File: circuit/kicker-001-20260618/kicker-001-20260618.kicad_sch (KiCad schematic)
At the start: 64 parts, among them J1 Solenoid_{Stroke}, J2 Solenoid_{Chip}, J3 Drribler_{Front}, J4 Conn_Relay, J6 Voltmeter, Q1 BSS138, Q2 TJ15S06M3L, Q3 Q_Photo_CE, Q4 MTB010N06RJ3, Q5 MTB010N06RJ3, U1 NOT, U10 TLP2361, U11 AND, U12 AND, U2 TLP2361, U3 XL6009E1, U4 NOT, U5 NOT, U6 DRV8874, U7 NOT, U8 NOT, U9 TLP2361

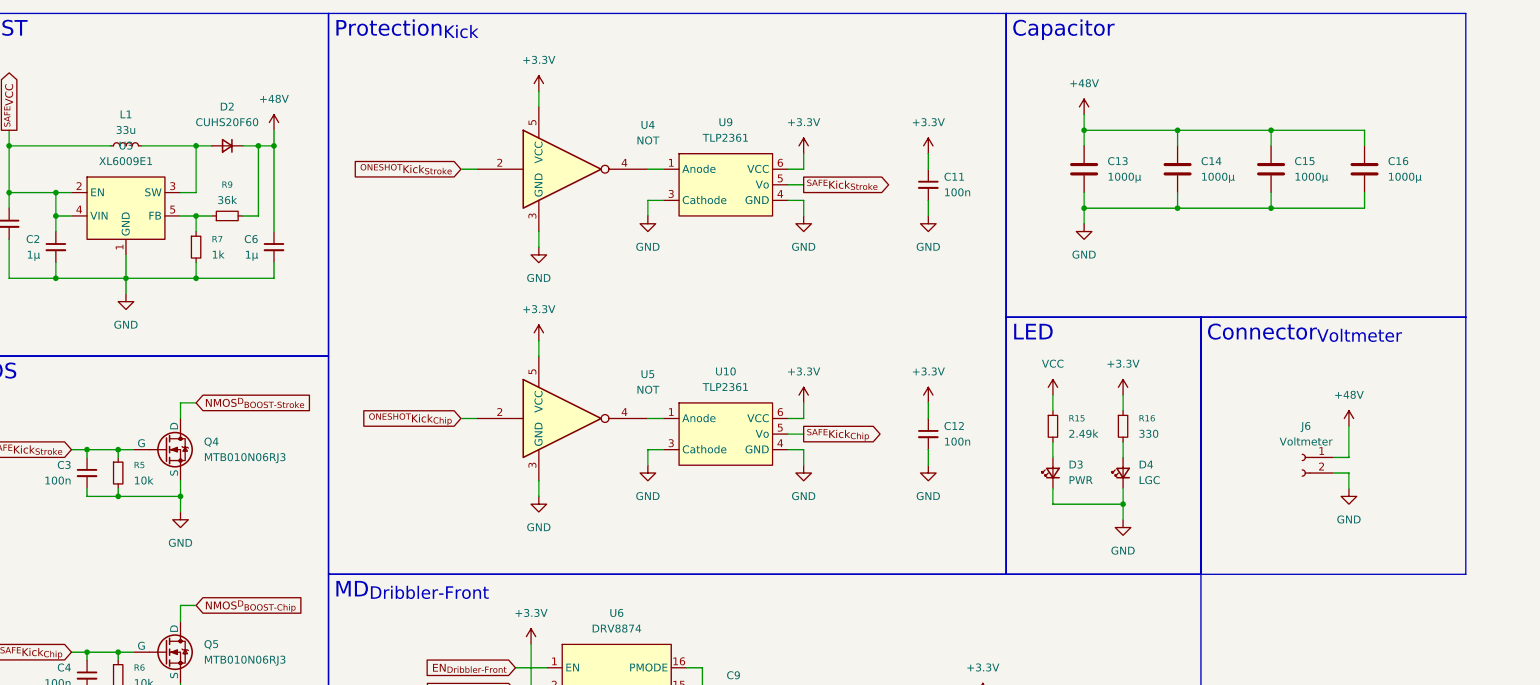
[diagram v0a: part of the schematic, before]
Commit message: Update キッカー基板のボード図完成させた、DRは一日おいてから
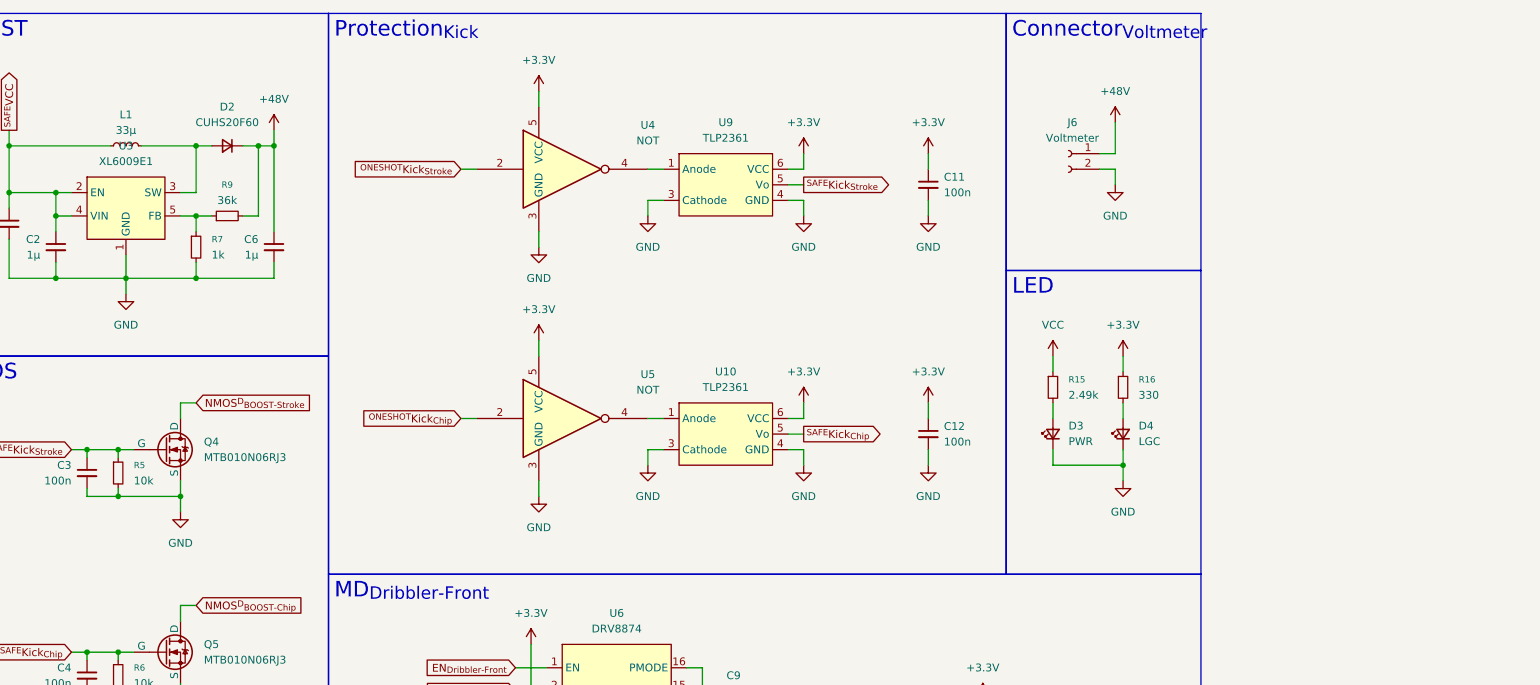
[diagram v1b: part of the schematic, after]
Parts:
- removed C13, C14, C15, C16: 1000μ, Capacitor_THT:C_Radial_D12.5mm_H25.0mm_P5.00mm, symbol Device:C
- C1, C10, C11, C12, C2, C3, C4, C5, C6, C7, C8, C9: footprint Capacitor_SMD:C_0603_1608Metric -> Capacitor_SMD:C_0805_2012Metric
- L1: value 33u -> 33μ
- R1, R10, R11, R12, R13, R14, R15, R16, R17, R2, R3, R4, R5, R6, R7, R8, R9: footprint Resistor_SMD:R_0603_1608Metric -> Resistor_SMD:R_0805_2012Metric
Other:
- moved on the sheet: D3, D4, J6, R15, R16

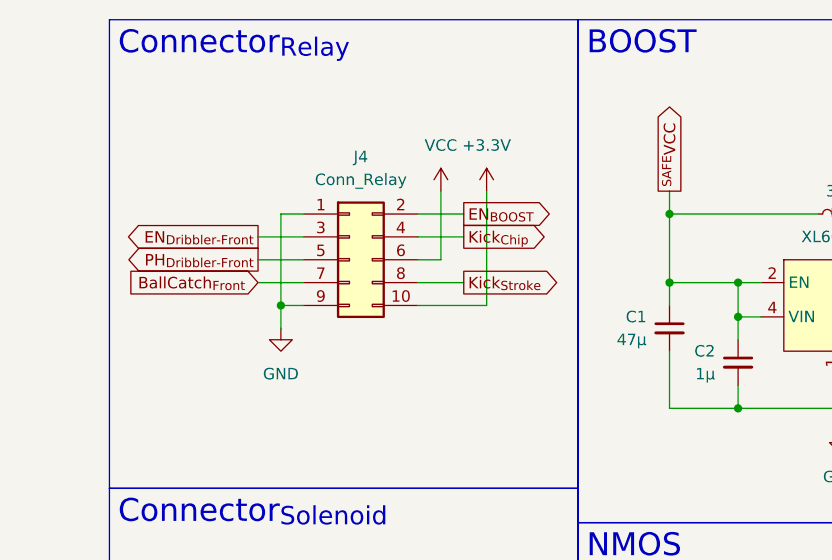
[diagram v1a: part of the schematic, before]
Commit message: Update キッカー基板のピンソケット→ピンヘッダ変更
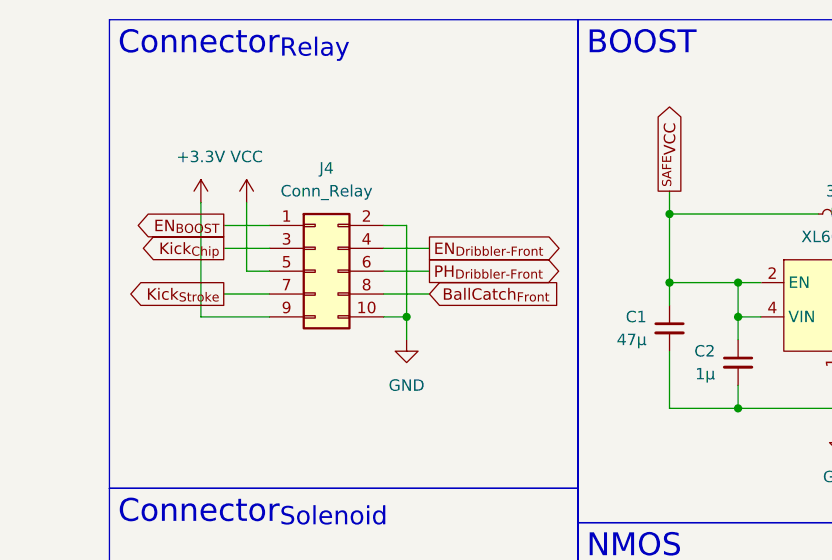
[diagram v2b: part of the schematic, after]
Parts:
- J4: footprint Connector_PinSocket_2.54mm:PinSocket_2x05_P2.54mm_Vertical -> Connector_PinHeader_2.54mm:PinHeader_2x05_P2.54mm_Vertical
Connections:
- net +3.3V: now also J4.9 (Pin_9); no longer J4.10 (Pin_10)
- net BallCatch_{Front}: now also J4.8 (Pin_8); no longer J4.7 (Pin_7)
- net EN_{BOOST}: now also J4.1 (Pin_1); no longer J4.2 (Pin_2)
- net EN_{Dribbler-Front}: now also J4.4 (Pin_4); no longer J4.3 (Pin_3)
- net GND: now also J4.10 (Pin_10), J4.2 (Pin_2); no longer J4.1 (Pin_1), J4.9 (Pin_9)
- net Kick_{Chip}: now also J4.3 (Pin_3); no longer J4.4 (Pin_4)
- net Kick_{Stroke}: now also J4.7 (Pin_7); no longer J4.8 (Pin_8)
- net PH_{Dribbler-Front}: now also J4.6 (Pin_6); no longer J4.5 (Pin_5)
- net VCC: now also J4.5 (Pin_5); no longer J4.6 (Pin_6)
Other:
- moved on the sheet: J4
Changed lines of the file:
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@@
 	)
 	(junction
-		(at 31.75 44.45)
+		(at 45.72 45.72)
 		(diameter 0)
 		(color 0 0 0 0)
@@
 	(wire
 		(pts
-			(xy 46.99 34.29) (xy 52.07 34.29)
+			(xy 30.48 35.56) (xy 25.4 35.56)
 		)
 		(stroke
@@
 	(wire
 		(pts
-			(xy 46.99 44.45) (xy 54.61 44.45)
+			(xy 30.48 45.72) (xy 22.86 45.72)
 		)
 		(stroke
@@
 	(wire
 		(pts
-			(xy 49.53 31.75) (xy 49.53 39.37)
+			(xy 27.94 33.02) (xy 27.94 40.64)
 		)
 		(stroke
@@
 	(wire
 		(pts
-			(xy 29.21 39.37) (xy 34.29 39.37)
+			(xy 48.26 40.64) (xy 43.18 40.64)
 		)
 		(stroke
@@
 	(wire
 		(pts
-			(xy 49.53 39.37) (xy 46.99 39.37)
+			(xy 27.94 40.64) (xy 30.48 40.64)
 		)
 		(stroke
@@
 	(wire
 		(pts
-			(xy 31.75 34.29) (xy 31.75 44.45)
+			(xy 45.72 35.56) (xy 45.72 45.72)
 		)
 		(stroke
@@
 	(wire
 		(pts
-			(xy 52.07 36.83) (xy 46.99 36.83)
+			(xy 25.4 38.1) (xy 30.48 38.1)
 		)
 		(stroke
@@
 	(wire
 		(pts
-			(xy 31.75 44.45) (xy 31.75 46.99)
+			(xy 45.72 45.72) (xy 45.72 48.26)
 		)
 		(stroke
@@
 	(wire
 		(pts
-			(xy 29.21 36.83) (xy 34.29 36.83)
+			(xy 48.26 38.1) (xy 43.18 38.1)
 		)
 		(stroke
@@
 	(wire
 		(pts
-			(xy 34.29 34.29) (xy 31.75 34.29)
+			(xy 43.18 35.56) (xy 45.72 35.56)
 		)
 		(stroke
@@
 	(wire
 		(pts
-			(xy 54.61 31.75) (xy 54.61 44.45)
+			(xy 22.86 33.02) (xy 22.86 45.72)
 		)
 		(stroke
@@
 	(wire
 		(pts
-			(xy 31.75 44.45) (xy 34.29 44.45)
+			(xy 45.72 45.72) (xy 43.18 45.72)
 		)
 		(stroke
@@
 	(wire
 		(pts
-			(xy 52.07 41.91) (xy 46.99 41.91)
+			(xy 25.4 43.18) (xy 30.48 43.18)
 		)
 		(stroke
@@
 	(wire
 		(pts
-			(xy 29.21 41.91) (xy 34.29 41.91)
+			(xy 48.26 43.18) (xy 43.18 43.18)
 		)
 		(stroke
@@
 	(global_label "PH_{Dribbler-Front}"
 		(shape output)
-		(at 29.21 39.37 180)
+		(at 48.26 40.64 0)
 		(fields_autoplaced yes)
 		(effects
@@
 				(size 1.27 1.27)
 			)
-			(justify right)
+			(justify left)
 		)
 		(property "Intersheetrefs" "${INTERSHEET_REFS}"
-			(at 15.1056 39.37 0)
+			(at 62.3644 40.64 0)
 			(hide yes)
 			(show_name no)
@@
 					(size 1.27 1.27)
 				)
-				(justify right)
+				(justify left)
 			)
 		)
@@
 	(global_label "EN_{BOOST}"
 		(shape output)
-		(at 52.07 34.29 0)
+		(at 25.4 35.56 180)
 		(fields_autoplaced yes)
 		(effects
@@
 				(size 1.27 1.27)
 			)
-			(justify left)
+			(justify right)
 		)
 		(property "Intersheetrefs" "${INTERSHEET_REFS}"
-			(at 62.0167 34.29 0)
+			(at 15.4533 35.56 0)
 			(hide yes)
 			(show_name no)
@@
 					(size 1.27 1.27)
 				)
-				(justify left)
+				(justify right)
 			)
 		)
@@
 	(global_label "EN_{Dribbler-Front}"
 		(shape output)
-		(at 29.21 36.83 180)
+		(at 48.26 38.1 0)
 		(fields_autoplaced yes)
 		(effects
@@
 				(size 1.27 1.27)
 			)
-			(justify right)
+			(justify left)
 		)
 		(property "Intersheetrefs" "${INTERSHEET_REFS}"
-			(at 15.1056 36.83 0)
+			(at 62.3644 38.1 0)
 			(hide yes)
 			(show_name no)
@@
 					(size 1.27 1.27)
 				)
-				(justify right)
+				(justify left)
 			)
 		)
@@
 	(global_label "Kick_{Stroke}"
 		(shape output)
-		(at 52.07 41.91 0)
+		(at 25.4 43.18 180)
 		(fields_autoplaced yes)
 		(effects
@@
 				(size 1.27 1.27)
 			)
-			(justify left)
+			(justify right)
 		)
 		(property "Intersheetrefs" "${INTERSHEET_REFS}"
-			(at 63.3294 41.91 0)
+			(at 14.1406 43.18 0)
 			(hide yes)
 			(show_name no)
@@
 					(size 1.27 1.27)
 				)
-				(justify left)
+				(justify right)
 			)
 		)
@@
 	(global_label "BallCatch_{Front}"
 		(shape input)
-		(at 29.21 41.91 180)
+		(at 48.26 43.18 0)
 		(fields_autoplaced yes)
 		(effects
@@
 				(size 1.27 1.27)
 			)
-			(justify right)
+			(justify left)
 		)
 		(property "Intersheetrefs" "${INTERSHEET_REFS}"
-			(at 13.7668 41.91 0)
+			(at 63.7032 43.18 0)
 			(hide yes)
 			(show_name no)
@@
 					(size 1.27 1.27)
 				)
-				(justify right)
+				(justify left)
 			)
 		)
@@
 	(global_label "Kick_{Chip}"
 		(shape output)
-		(at 52.07 36.83 0)
+		(at 25.4 38.1 180)
 		(fields_autoplaced yes)
 		(effects
@@
 				(size 1.27 1.27)
 			)
-			(justify left)
+			(justify right)
 		)
 		(property "Intersheetrefs" "${INTERSHEET_REFS}"
-			(at 62.384 36.83 0)
+			(at 15.086 38.1 0)
 			(hide yes)
 			(show_name no)
@@
 					(size 1.27 1.27)
 				)
-				(justify left)
+				(justify right)
 			)
 		)
@@
 	(symbol
 		(lib_id "power:GND")
-		(at 31.75 46.99 0)
+		(at 45.72 48.26 0)
+		(mirror y)
 		(unit 1)
 		(body_style 1)
@@
 		(fields_autoplaced yes)
 		(property "Reference" "#PWR02"
-			(at 31.75 53.34 0)
+			(at 45.72 54.61 0)
 			(hide yes)
 			(show_name no)
@@
 		)
 		(property "Value" "GND"
-			(at 31.75 52.07 0)
+			(at 45.72 53.34 0)
 			(show_name no)
 			(do_not_autoplace no)
@@
 		)
 		(property "Footprint" ""
-			(at 31.75 46.99 0)
+			(at 45.72 48.26 0)
 			(hide yes)
 			(show_name no)
@@
 		)
 		(property "Datasheet" ""
-			(at 31.75 46.99 0)
+			(at 45.72 48.26 0)
 			(hide yes)
 			(show_name no)
@@
 		)
 		(property "Description" "Power symbol creates a global label with name \"GND\" , ground"
-			(at 31.75 46.99 0)
+			(at 45.72 48.26 0)
 			(hide yes)
 			(show_name no)
@@
 	(symbol
 		(lib_id "Connector_Generic:Conn_02x05_Odd_Even")
-		(at 39.37 39.37 0)
+		(at 35.56 40.64 0)
 		(unit 1)
 		(body_style 1)
@@
 		(in_pos_files yes)
 		(dnp no)
-		(fields_autoplaced yes)
 		(property "Reference" "J4"
-			(at 40.64 27.94 0)
+			(at 36.83 29.21 0)
 			(show_name no)
 			(do_not_autoplace no)
@@
 		)
 		(property "Value" "Conn_Relay"
-			(at 40.64 30.48 0)
+			(at 36.83 31.75 0)
 			(show_name no)
 			(do_not_autoplace no)
@@
 			)
 		)
-		(property "Footprint" "Connector_PinSocket_2.54mm:PinSocket_2x05_P2.54mm_Vertical"
-			(at 39.37 39.37 0)
+		(property "Footprint" "Connector_PinHeader_2.54mm:PinHeader_2x05_P2.54mm_Vertical"
+			(at 35.56 40.64 0)
 			(hide yes)
 			(show_name no)
@@
 		)
 		(property "Datasheet" ""
-			(at 39.37 39.37 0)
+			(at 35.56 40.64 0)
 			(hide yes)
 			(show_name no)
@@
 		)
 		(property "Description" "Generic connector, double row, 02x05, odd/even pin numbering scheme (row 1 odd numbers, row 2 even numbers), script generated (kicad-library-utils/schlib/autogen/connector/)"
-			(at 39.37 39.37 0)
+			(at 35.56 40.64 0)
 			(hide yes)
 			(show_name no)
@@
 	(symbol
 		(lib_id "power:VCC")
-		(at 49.53 31.75 0)
+		(at 27.94 33.02 0)
+		(mirror y)
 		(unit 1)
 		(body_style 1)
@@
 		(fields_autoplaced yes)
 		(property "Reference" "#PWR01"
-			(at 49.53 35.56 0)
+			(at 27.94 36.83 0)
 			(hide yes)
 			(show_name no)
@@
 		)
 		(property "Value" "VCC"
-			(at 49.53 26.67 0)
+			(at 27.94 27.94 0)
 			(show_name no)
 			(do_not_autoplace no)
@@
 		)
 		(property "Footprint" ""
-			(at 49.53 31.75 0)
+			(at 27.94 33.02 0)
 			(hide yes)
 			(show_name no)
@@
 		)
 		(property "Datasheet" ""
-			(at 49.53 31.75 0)
+			(at 27.94 33.02 0)
 			(hide yes)
 			(show_name no)
@@
 		)
 		(property "Description" "Power symbol creates a global label with name \"VCC\""
-			(at 49.53 31.75 0)
+			(at 27.94 33.02 0)
 			(hide yes)
 			(show_name no)
@@
 	(symbol
 		(lib_id "power:+3.3V")
-		(at 54.61 31.75 0)
+		(at 22.86 33.02 0)
+		(mirror y)
 		(unit 1)
 		(body_style 1)
@@
 		(fields_autoplaced yes)
 		(property "Reference" "#PWR07"
-			(at 54.61 35.56 0)
+			(at 22.86 36.83 0)
 			(hide yes)
 			(show_name no)
@@
 		)
 		(property "Value" "+3.3V"
-			(at 54.61 26.67 0)
+			(at 22.86 27.94 0)
 			(show_name no)
 			(do_not_autoplace no)
@@
 		)
 		(property "Footprint" ""
-			(at 54.61 31.75 0)
+			(at 22.86 33.02 0)
 			(hide yes)
 			(show_name no)
@@
 		)
 		(property "Datasheet" ""
-			(at 54.61 31.75 0)
+			(at 22.86 33.02 0)
 			(hide yes)
 			(show_name no)
@@
 		)
 		(property "Description" "Power symbol creates a global label with name \"+3.3V\""
-			(at 54.61 31.75 0)
+			(at 22.86 33.02 0)
 			(hide yes)
 			(show_name no)
